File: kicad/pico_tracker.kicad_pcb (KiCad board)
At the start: 2 copper layers, 92.9 x 125.4 mm, 29 parts, among them J1 MIDI_OUT, J10 DclassAMP, J11 MASTER_VOLUME, J2 MIDI_IN, J3 MIDI_IN_A_B_VCC, J4 MIDI_IN_A_B_DATA, J5 MIDI_OUT_A_B_VCC, J6 MIDI_OUT_A_B_DATA, J7 DISPLAY, J8 SDCARD, J9 KILL_SWITCH, SW1 SW_PG1350, SW2 SW_PG1350, SW3 SW_PG1350, SW4 SW_PG1350, SW5 SW_PG1350, SW6 SW_PG1350, SW7 SW_PG1350, SW8 SW_PG1350, SW9 SW_PG1350, U1 Pico, U2 6N138, U3 PCM5102_Module

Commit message: Add files via upload
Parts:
- removed J11: MASTER_VOLUME, Connector_PinHeader_2.54mm:PinHeader_2x03_P2.54mm_Vertical_SMD
- added G1: LOGO, pico_tracker:logo_silk, F.Cu at (111.2, 92.5)
- J9: value KILL_SWITCH -> SPEAKER KILLSWITCH
- moved J9 89.5 mm to (107.1, 68.5)
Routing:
- net LOUT: track 110.5 -> 0.00 mm
- net ROUT: track 89.0 -> 0.00 mm
- net L_AMP: track 63.4 -> 0.00 mm
- net R_AMP: track 55.3 -> 0.00 mm
- net KILL_SWITCH: track 42.7 -> 77.3 mm
- net PLAY: track 103.7 -> 74.0 mm
- net DOWN: track 75.5 -> 91.9 mm
- net RIGHT: track 62.8 -> 75.0 mm
- net D1: track 38.6 -> 26.7 mm
- net SO: track 30.9 -> 39.9 mm
- net DP7: track 34.7 -> 43.5 mm
- net VCC: track 175.5 -> 167.8 mm
- net DP3: track 50.1 -> 42.9 mm
- net DAT2: track 23.6 -> 30.4 mm
- net SI: track 31.9 -> 38.3 mm
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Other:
- outline, holes or cut-outs redrawn

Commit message: Add files via upload
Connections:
- J1 pad 1: (no net) -> GND
- J1 pad 2: (no net) -> GND
- J1 pad 3: (no net) -> Net-(J1-PadR)
- J1 pad 4: (no net) -> Net-(J1-PadT)
- J2 pad 1: (no net) -> GND
- J2 pad 2: (no net) -> GND
- J2 pad 3: (no net) -> Net-(J2-PadR)
- J2 pad 4: (no net) -> Net-(J2-PadT)
- REF1 pad 1: LOUT -> L_AMP
- REF1 pad 3: ROUT -> R_AMP
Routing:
- net R_AMP: track 0.00 -> 37.9 mm
- net L_AMP: track 0.00 -> 36.4 mm
- net Net-(J1-PadR): track 9.02 -> 28.5 mm
- net DOWN: track 91.9 -> 74.7 mm
- net DP7: track 43.5 -> 28.3 mm
- net Net-(J2-PadR): track 9.04 -> 22.7 mm
- net Net-(J2-PadT): track 12.1 -> 25.0 mm
- net RIGHT: track 75.0 -> 62.8 mm
- net VCC: track 167.8 -> 178.8 mm
- net Net-(J1-PadT): track 9.05 -> 19.3 mm
- net RX: track 76.3 -> 66.6 mm, vias 0 -> 1
- net TX: track 72.2 -> 63.3 mm
- net DP5: track 33.9 -> 41.9 mm
- net CLK: track 40.5 -> 46.6 mm
- net DP4: track 34.8 -> 39.8 mm
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
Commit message: Add files via upload
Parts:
- J10: moved to F.Cu
- moved J10 20.3 mm to (159.9, 76.2)
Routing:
- net TX: track 63.3 -> 77.6 mm
- net RIGHT: track 62.8 -> 73.8 mm
- net KILL_SWITCH: track 77.3 -> 67.0 mm
- net RX: track 66.6 -> 75.9 mm, vias 1 -> 0
- net PLAY: track 74.1 -> 65.6 mm
- net DP5: track 41.9 -> 34.3 mm
- net GND: track 7.47 -> 0.00 mm, vias 2 -> 1
- net CLK: track 46.6 -> 40.5 mm
- net A: track 47.9 -> 53.8 mm
- net R_AMP: track 37.9 -> 33.2 mm
- net DP4: track 39.8 -> 35.1 mm
- net L_AMP: track 36.4 -> 39.6 mm
- net BCK: track 45.8 -> 42.6 mm
- net VCC: track 178.8 -> 175.6 mm
- net AGND: track 45.5 -> 43.6 mm
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
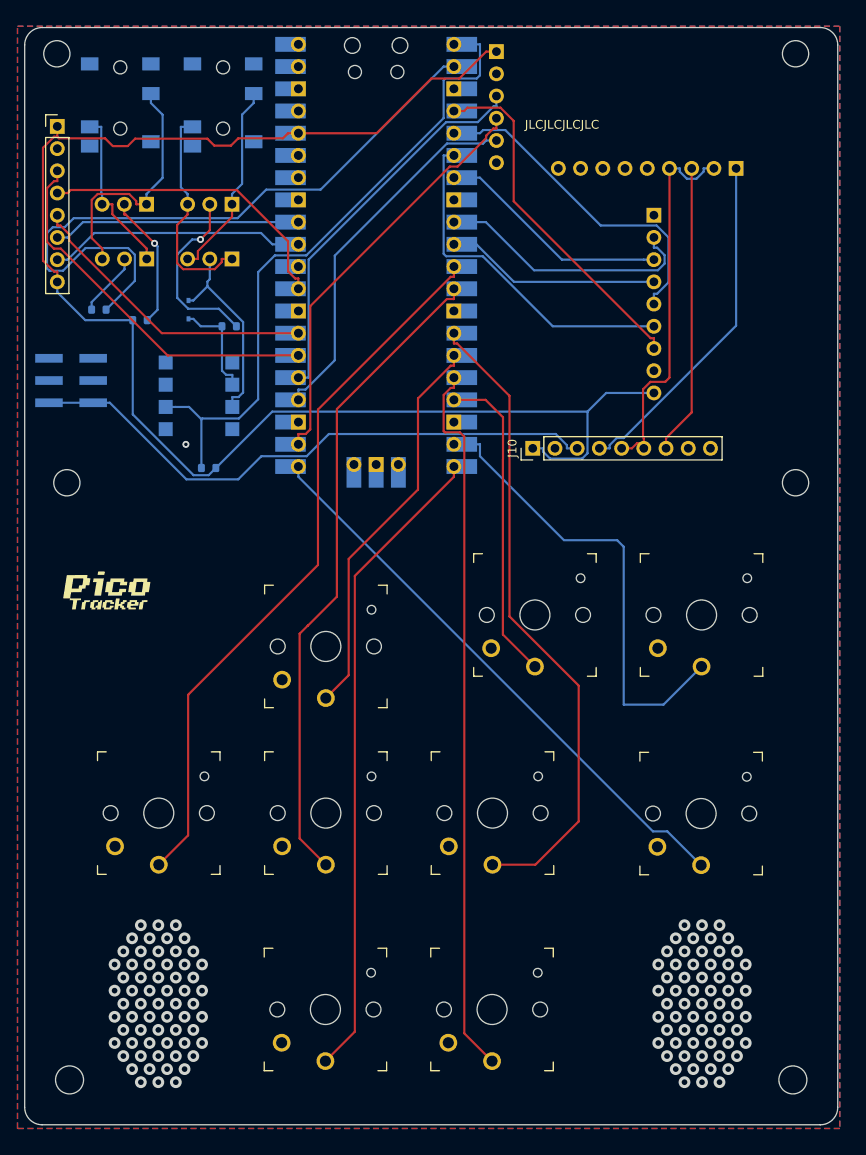
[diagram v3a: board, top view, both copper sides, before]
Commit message: fix: 6N138 VCC connexion and RX/TX pins flip
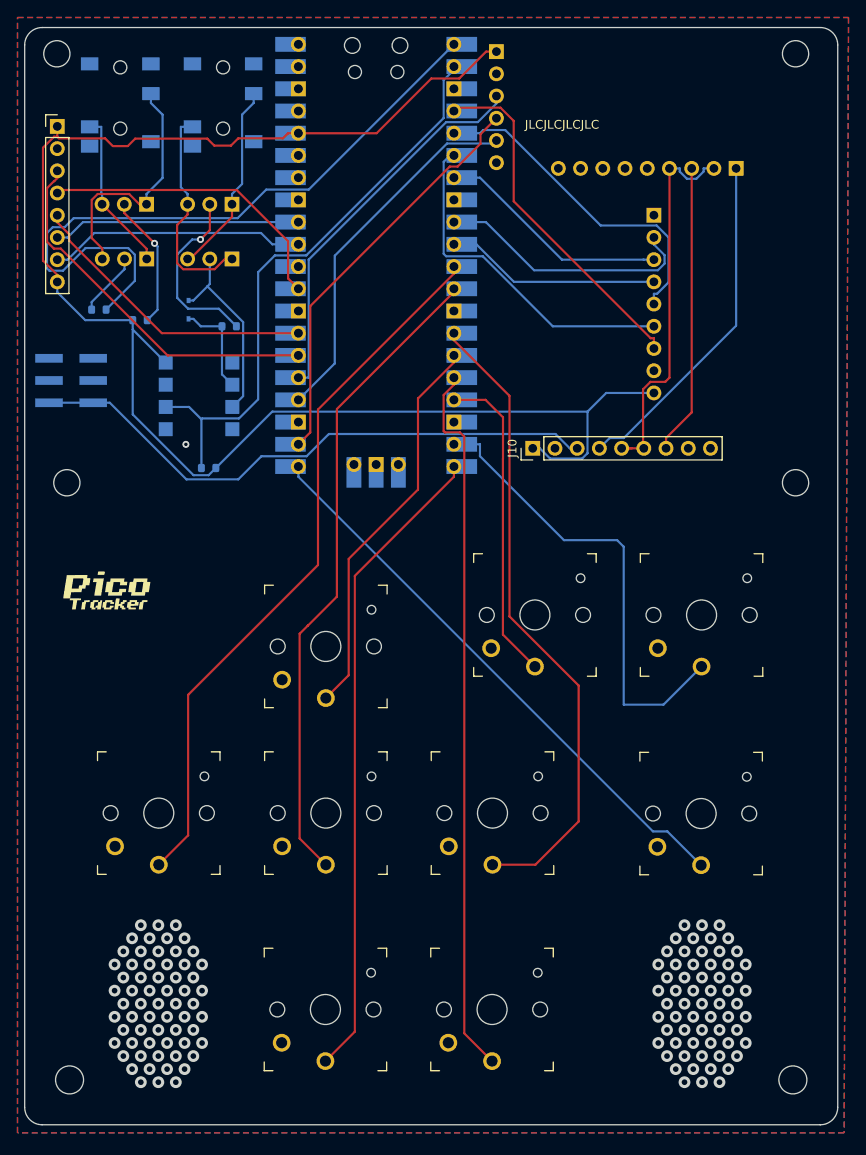
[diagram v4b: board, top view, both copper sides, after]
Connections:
- U1 pad 1: RX -> TX
- U1 pad 2: TX -> RX
- U2 pad 8: VCC5 -> VCC
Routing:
- net RX: track 75.9 -> 67.1 mm
- net VCC: track 175.6 -> 180.5 mm
- net TX: track 77.6 -> 78.7 mm
- net AGND: track 43.6 -> 44.5 mm
- net DIN: track 47.9 -> 47.2 mm
- net Net-(J1-PadT): track 19.3 -> 18.6 mm
- net Net-(J2-PadR): track 22.7 -> 22.2 mm

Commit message: chore: generate gerber files
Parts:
- J9: value SPEAKER KILLSWITCH -> KILL_SWITCH
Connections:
- J1 pad 1: GND -> (no net)
- J1 pad 2: GND -> (no net)
- J1 pad 3: Net-(J1-PadR) -> (no net)
- J1 pad 4: Net-(J1-PadT) -> (no net)
- J2 pad 1: GND -> (no net)
- J2 pad 2: GND -> (no net)
- J2 pad 3: Net-(J2-PadR) -> (no net)
- J2 pad 4: Net-(J2-PadT) -> (no net)
- J3 pad 1: Net-(J2-PadR) -> Net-(J3-Pin_1)
- J3 pad 3: Net-(J2-PadT) -> Net-(J3-Pin_3)
- J4 pad 1: Net-(J2-PadT) -> Net-(J3-Pin_3)
- J4 pad 3: Net-(J2-PadR) -> Net-(J3-Pin_1)
- J5 pad 1: Net-(J1-PadR) -> Net-(J5-Pin_1)
- J5 pad 3: Net-(J1-PadT) -> Net-(J5-Pin_3)
- J6 pad 1: Net-(J1-PadT) -> Net-(J5-Pin_3)
- J6 pad 3: Net-(J1-PadR) -> Net-(J5-Pin_1)
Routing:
- net Net-(J5-Pin_1): track 0.00 -> 28.2 mm
- net Net-(J1-PadR): track 28.2 -> 0.00 mm
- net Net-(J3-Pin_3): track 0.00 -> 24.8 mm
- net Net-(J2-PadT): track 24.8 -> 0.00 mm
- net Net-(J3-Pin_1): track 0.00 -> 22.2 mm
- net Net-(J2-PadR): track 22.2 -> 0.00 mm
- net Net-(J5-Pin_3): track 0.00 -> 18.6 mm
- net Net-(J1-PadT): track 18.6 -> 0.00 mm

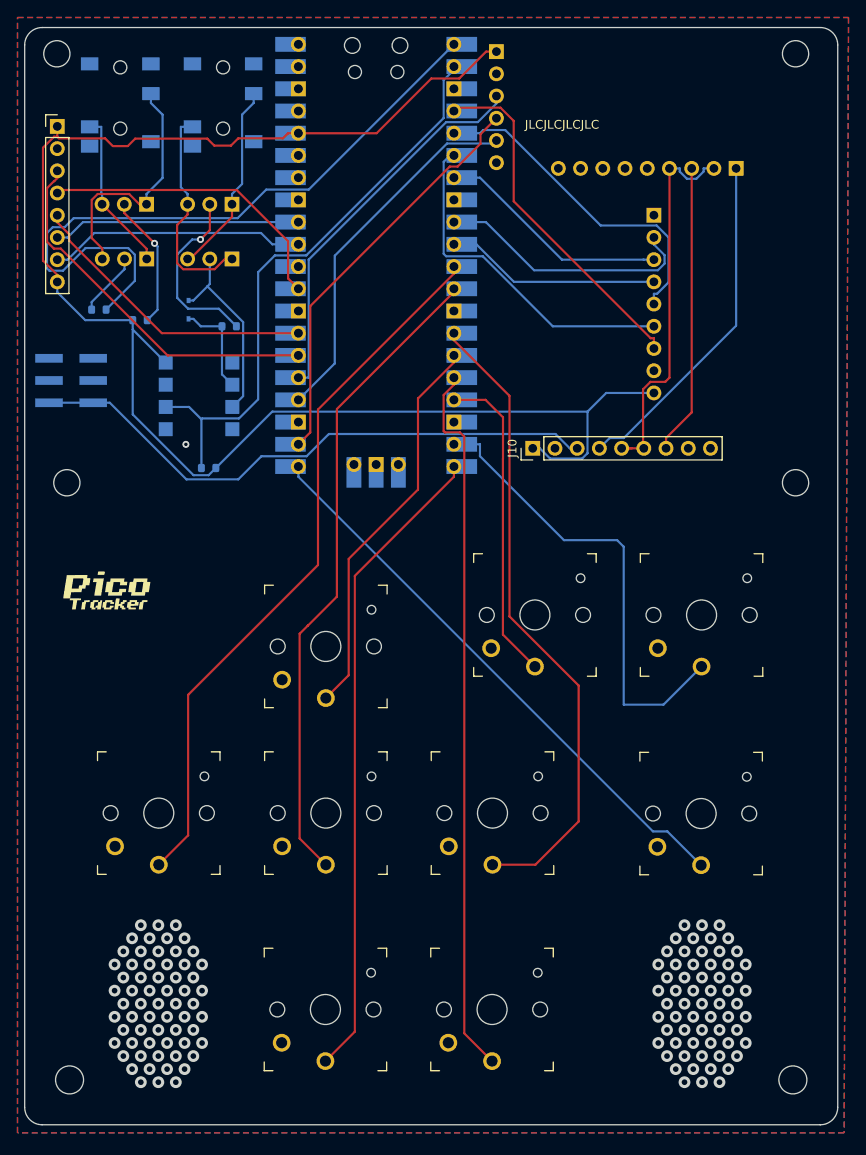
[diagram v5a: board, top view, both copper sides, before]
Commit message: fix: add 10k resistor to pin 7
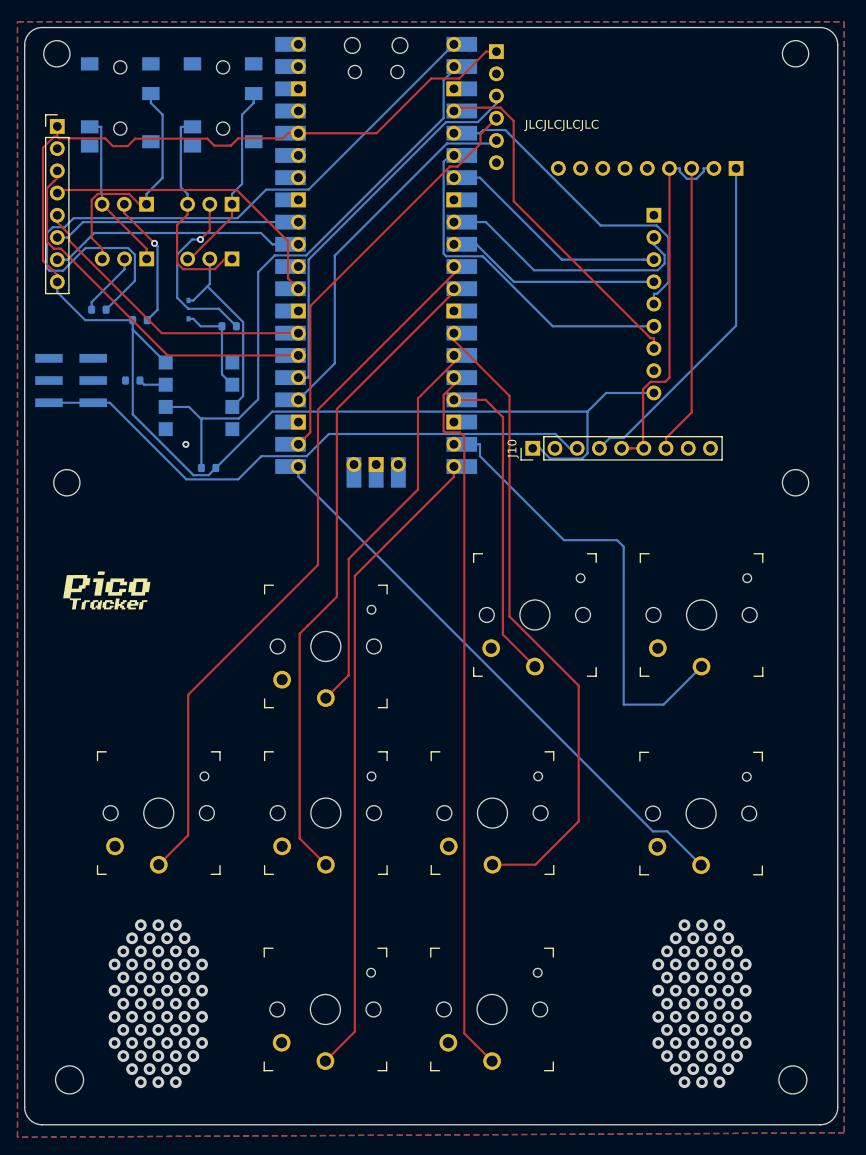
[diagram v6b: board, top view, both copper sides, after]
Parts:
- added R5: 10k, Resistor_SMD:R_0603_1608Metric, B.Cu at (114.2, 68.5)
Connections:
- U2 pad 7: unconnected-(U2-VO1-Pad7) -> Net-(U2-VO1)
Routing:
- net Net-(U2-VO1): track 0.00 -> 3.14 mm
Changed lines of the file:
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@@
 	(net 70 "unconnected-(U2-NC-Pad1)")
 	(net 71 "unconnected-(U2-NC-Pad4)")
-	(net 72 "unconnected-(U2-VO1-Pad7)")
+	(net 72 "Net-(U2-VO1)")
 	(footprint "Button_Switch_Keyboard:SW_PG1350"
 		(layer "F.Cu")
@@
 			(size 1.6 1.6)
 			(layers "B.Cu" "B.Mask" "B.Paste")
-			(net 72 "unconnected-(U2-VO1-Pad7)")
+			(net 72 "Net-(U2-VO1)")
 			(pinfunction "VO1")
-			(pintype "passive+no_connect")
+			(pintype "passive")
 		)
 		(pad "8" smd rect
@@
 	(footprint "Resistor_SMD:R_0603_1608Metric"
 		(layer "B.Cu")
+		(at 114.175 68.5)
+		(descr "Resistor SMD 0603 (1608 Metric), square (rectangular) end terminal, IPC-7351 nominal, (Body size source: IPC-SM-782 page 72, https://www.pcb-3d.com/wordpress/wp-content/uploads/ipc-sm-782a_amendment_1_and_2.pdf), generated with kicad-footprint-generator")
+		(tags "resistor")
+		(property "Reference" "R5"
+			(at 0 1.43 0)
+			(layer "B.SilkS")
+			(effects
+				(font
+					(size 1 1)
+					(thickness 0.15)
+				)
+				(justify mirror)
+			)
+		)
+		(property "Value" "10k"
+			(at 0 -1.43 0)
+			(layer "B.Fab")
+			(effects
+				(font
+					(size 1 1)
+					(thickness 0.15)
+				)
+				(justify mirror)
+			)
+		)
+		(property "Datasheet" "~"
+			(at 0 0 0)
+			(layer "B.Fab")
+			(hide yes)
+			(effects
+				(font
+					(size 1.27 1.27)
+					(thickness 0.15)
+				)
+				(justify mirror)
+			)
+		)
+		(property "Description" ""
+			(at 0 0 0)
+			(layer "B.Fab")
+			(hide yes)
+			(effects
+				(font
+					(size 1.27 1.27)
+					(thickness 0.15)
+				)
+				(justify mirror)
+			)
+		)
+		(property ki_fp_filters "R_*")
+		(sheetname "/")
+		(sheetfile "pico_tracker.kicad_sch")
+		(attr smd)
+		(fp_line
+			(start -0.237258 -0.5225)
+			(end 0.237258 -0.5225)
+			(stroke
+				(width 0.12)
+				(type solid)
+			)
+			(layer "B.SilkS")
+		)
+		(fp_line
+			(start -0.237258 0.5225)
+			(end 0.237258 0.5225)
+			(stroke
+				(width 0.12)
+				(type solid)
+			)
+			(layer "B.SilkS")
+		)
+		(fp_rect
+			(start -1.48 0.73)
+			(end 1.48 -0.73)
+			(stroke
+				(width 0.05)
+				(type solid)
+			)
+			(fill no)
+			(layer "B.CrtYd")
+		)
+		(fp_rect
+			(start -0.8 0.4125)
+			(end 0.8 -0.4125)
+			(stroke
+				(width 0.1)
+				(type solid)
+			)
+			(fill no)
+			(layer "B.Fab")
+		)
+		(fp_text user "${REFERENCE}"
+			(at 0 0 0)
+			(layer "B.Fab")
+			(effects
+				(font
+					(size 0.4 0.4)
+					(thickness 0.06)
+				)
+				(justify mirror)
+			)
+		)
+		(pad "1" smd roundrect
+			(at -0.825 0)
+			(size 0.8 0.95)
+			(layers "B.Cu" "B.Mask" "B.Paste")
+			(roundrect_rratio 0.25)
+			(net 11 "GND")
+			(pintype "passive")
+		)
+		(pad "2" smd roundrect
+			(at 0.825 0)
+			(size 0.8 0.95)
+			(layers "B.Cu" "B.Mask" "B.Paste")
+			(roundrect_rratio 0.25)
+			(net 72 "Net-(U2-VO1)")
+			(pintype "passive")
+		)
+		(embedded_fonts no)
+		(model "${KICAD9_3DMODEL_DIR}/Resistor_SMD.3dshapes/R_0603_1608Metric.step"
+			(offset
+				(xyz 0 0 0)
+			)
+			(scale
+				(xyz 1 1 1)
+			)
+			(rotate
+				(xyz 0 0 0)
+			)
+		)
+	)
+	(footprint "Resistor_SMD:R_0603_1608Metric"
+		(layer "B.Cu")
 		(at 115 61.6)
 		(descr "Resistor SMD 0603 (1608 Metric), square (rectangular) end terminal, IPC_7351 nominal, (Body size source: IPC-SM-782 page 72, https://www.pcb-3d.com/wordpress/wp-content/uploads/ipc-sm-782a_amendment_1_and_2.pdf), generated with kicad-footprint-generator")
@@
 		(net 58)
 	)
+	(segment
+		(start 115.48 68.98)
+		(end 115 68.5)
+		(width 0.25)
+		(layer "B.Cu")
+		(net 72)
+	)
+	(segment
+		(start 117.94 68.98)
+		(end 115.48 68.98)
+		(width 0.25)
+		(layer "B.Cu")
+		(net 72)
+	)
 	(zone
 		(net 11)
@@
 		(layer "F.Cu")
 		(hatch edge 0.5)
-		(priority 1)
 		(connect_pads
 			(clearance 0.508)
@@
 		(polygon
 			(pts
-				(xy 101 27) (xy 196 27) (xy 195.5 154.5) (xy 101 154.5)
+				(xy 101 27.5) (xy 195.5 27.5) (xy 195.5 154.5) (xy 101 155)
 			)
 		)
@@
 		(layer "B.Cu")
 		(hatch edge 0.5)
+		(priority 1)
 		(connect_pads
 			(clearance 0.508)
@@
 		(polygon
 			(pts
-				(xy 101 27) (xy 196 27) (xy 195.5 154.5) (xy 101 154.5)
+				(xy 101 27.5) (xy 195.5 27.5) (xy 195.5 154.5) (xy 101 155)
 			)
 		)
